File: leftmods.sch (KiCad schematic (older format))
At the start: 17 parts

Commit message: Get rid of LM5 and SP1 for 6.5U bottom row
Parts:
- removed K_LM5: MX-1.5U, MX_Alps_Hybrid:MX-1.5U, symbol MX-1.5U
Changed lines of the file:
@@
-$EndComp
-$Comp
-L MX-1.5U K_LM5
-U 1 1 591D0916
-P 3700 3100
-F 0 "K_LM5" H 3700 3225 60  0000 C CNN
-F 1 "MX-1.5U" H 3700 3150 20  0000 C CNN
-F 2 "MX_Alps_Hybrid:MX-1.5U" H 3675 3075 60  0001 C CNN
-F 3 "" H 3675 3075 60  0001 C CNN
-	1    3700 3100
-	1    0    0    -1
 $EndComp
 $Comp

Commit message: Remove true HHKB row (LM8/9, SP15, RM15/16)
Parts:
- removed K_LM8: MX-1U, MX_Alps_Hybrid:MX-1U, symbol MX-1U
- removed K_LM9: MX-1.5U, MX_Alps_Hybrid:MX-1.5U, symbol MX-1.5U
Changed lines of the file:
@@
-$EndComp
-$Comp
-L MX-1U K_LM8
-U 1 1 594A5358
-P 3700 3675
-F 0 "K_LM8" H 3700 3800 60  0000 C CNN
-F 1 "MX-1U" H 3700 3725 20  0000 C CNN
-F 2 "MX_Alps_Hybrid:MX-1U" H 3675 3650 60  0001 C CNN
-F 3 "" H 3675 3650 60  0001 C CNN
-	1    3700 3675
-	1    0    0    -1
-$EndComp
-$Comp
-L MX-1.5U K_LM9
-U 1 1 594A64BB
-P 4250 3675
-F 0 "K_LM9" H 4250 3800 60  0000 C CNN
-F 1 "MX-1.5U" H 4250 3725 20  0000 C CNN
-F 2 "MX_Alps_Hybrid:MX-1.5U" H 4225 3650 60  0001 C CNN
-F 3 "" H 4225 3650 60  0001 C CNN
-	1    4250 3675
-	1    0    0    -1
 $EndComp
 $Comp

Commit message: Add in the Alps bottom row
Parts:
- K_LM10: footprint MX_Alps_Hybrid:MX-1.25U -> MX_Alps_Hybrid:ALPS-1.25U
- K_LM11: footprint MX_Alps_Hybrid:MX-1.5U -> MX_Alps_Hybrid:ALPS-1.5U
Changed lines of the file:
@@
 F 0 "K_LM11" H 4250 4375 60  0000 C CNN
 F 1 "MX-1.5U" H 4250 4300 20  0000 C CNN
-F 2 "MX_Alps_Hybrid:MX-1.5U" H 4225 4225 60  0001 C CNN
+F 2 "MX_Alps_Hybrid:ALPS-1.5U" H 4225 4225 60  0001 C CNN
 F 3 "" H 4225 4225 60  0001 C CNN
 	1    4250 4250
@@
 F 0 "K_LM10" H 3700 4375 60  0000 C CNN
 F 1 "MX-1.25U" H 3700 4300 20  0000 C CNN
-F 2 "MX_Alps_Hybrid:MX-1.25U" H 3675 4225 60  0001 C CNN
+F 2 "MX_Alps_Hybrid:ALPS-1.25U" H 3675 4225 60  0001 C CNN
 F 3 "" H 3675 4225 60  0001 C CNN
 	1    3700 4250

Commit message: Assign the footprints for every resistor and diode
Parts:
- DLM1, DLM2, DLM3: footprint (none) -> Diodes_SMD:D_SOD-323
- RLM1, RLM2, RLM3: footprint (none) -> Resistors_SMD:R_0603
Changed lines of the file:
@@
 F 0 "DLM2" H 3675 4725 50  0000 C CNN
 F 1 "1N4148WS" H 3675 4525 50  0000 C CNN
-F 2 "" H 3675 4625 50  0001 C CNN
+F 2 "Diodes_SMD:D_SOD-323" H 3675 4625 50  0001 C CNN
 F 3 "" H 3675 4625 50  0000 C CNN
 	1    3675 4625
@@
 F 0 "DLM3" H 4225 4725 50  0000 C CNN
 F 1 "1N4148WS" H 4225 4525 50  0000 C CNN
-F 2 "" H 4225 4625 50  0001 C CNN
+F 2 "Diodes_SMD:D_SOD-323" H 4225 4625 50  0001 C CNN
 F 3 "" H 4225 4625 50  0000 C CNN
 	1    4225 4625
@@
 F 0 "RLM1" V 3530 5800 50  0000 C CNN
 F 1 "2.2k" V 3450 5800 50  0000 C CNN
-F 2 "" V 3380 5800 50  0001 C CNN
+F 2 "Resistors_SMD:R_0603" V 3380 5800 50  0001 C CNN
 F 3 "" H 3450 5800 50  0000 C CNN
 	1    3450 5800
@@
 F 0 "RLM2" V 4080 5800 50  0000 C CNN
 F 1 "2.2k" V 4000 5800 50  0000 C CNN
-F 2 "" V 3930 5800 50  0001 C CNN
+F 2 "Resistors_SMD:R_0603" V 3930 5800 50  0001 C CNN
 F 3 "" H 4000 5800 50  0000 C CNN
 	1    4000 5800
@@
 F 0 "RLM3" V 4630 5800 50  0000 C CNN
 F 1 "2.2k" V 4550 5800 50  0000 C CNN
-F 2 "" V 4480 5800 50  0001 C CNN
+F 2 "Resistors_SMD:R_0603" V 4480 5800 50  0001 C CNN
 F 3 "" H 4550 5800 50  0000 C CNN
 	1    4550 5800
@@
 F 0 "DLM1" H 3125 4725 50  0000 C CNN
 F 1 "1N4148WS" H 3125 4525 50  0000 C CNN
-F 2 "" H 3125 4625 50  0001 C CNN
+F 2 "Diodes_SMD:D_SOD-323" H 3125 4625 50  0001 C CNN
 F 3 "" H 3125 4625 50  0000 C CNN
 	1    3125 4625

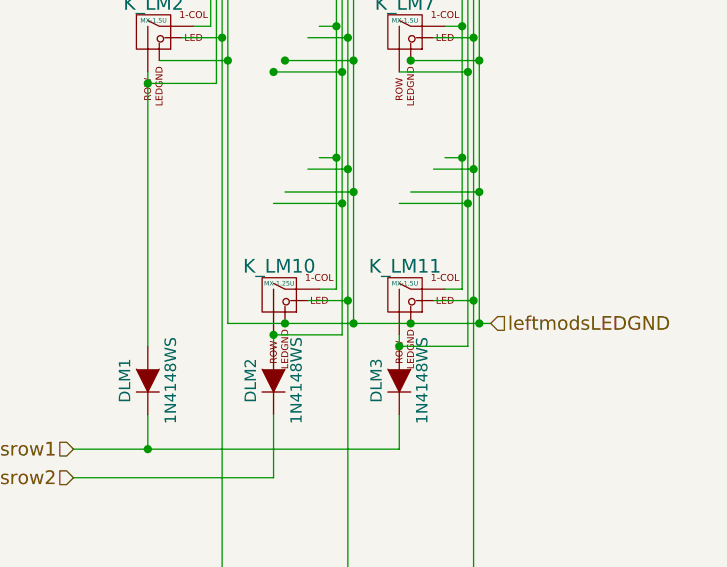
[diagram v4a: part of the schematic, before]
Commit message: Flipped schematic symbols for keys (except LS and bottom right mods)
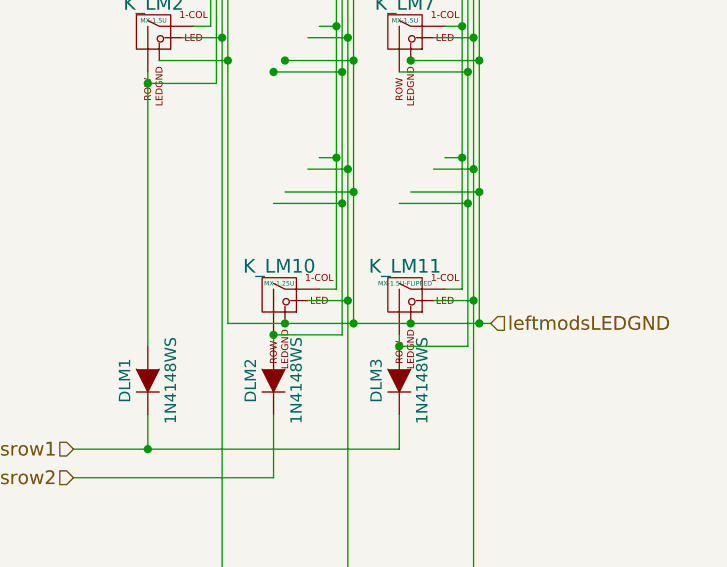
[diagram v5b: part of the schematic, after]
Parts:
- removed K_LM11: MX-1.5U, MX_Alps_Hybrid:ALPS-1.5U, symbol MX-1.5U
- added K_LM11: MX-1.5U-FLIPPED, symbol MX-1.5U-FLIPPED
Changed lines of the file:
@@
-$EndComp
-$Comp
-L MX-1.5U K_LM11
-U 1 1 594A6C8D
-P 4250 4250
-F 0 "K_LM11" H 4250 4375 60  0000 C CNN
-F 1 "MX-1.5U" H 4250 4300 20  0000 C CNN
-F 2 "MX_Alps_Hybrid:ALPS-1.5U" H 4225 4225 60  0001 C CNN
-F 3 "" H 4225 4225 60  0001 C CNN
-	1    4250 4250
-	1    0    0    -1
 $EndComp
 $Comp
@@
 Wire Wire Line
 	3675 5050 3675 4775
+$Comp
+L MX-1.5U-FLIPPED K_LM11
+U 1 1 598F2D66
+P 4250 4250
+F 0 "K_LM11" H 4250 4375 60  0000 C CNN
+F 1 "MX-1.5U-FLIPPED" H 4250 4300 20  0000 C CNN
+F 2 "" H 4225 4225 60  0001 C CNN
+F 3 "" H 4225 4225 60  0001 C CNN
+	1    4250 4250
+	1    0    0    -1
+$EndComp
 $EndSCHEMATC
